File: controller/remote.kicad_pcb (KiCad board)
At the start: 2 copper layers, 69 x 58.7 mm, 32 parts, among them J1 Conn_01x03, J2 Debug, J4 Conn_01x06, J8 Conn_01x08, J9 Conn_01x08, Q1 MMBT3904, Q2 MMBT3904, U1 74HC165, U2 74HC165, U3 NRF24L01_Breakout, U4 ADS7828, U5 ESP32-WROOM-32U, U6 MC130VX

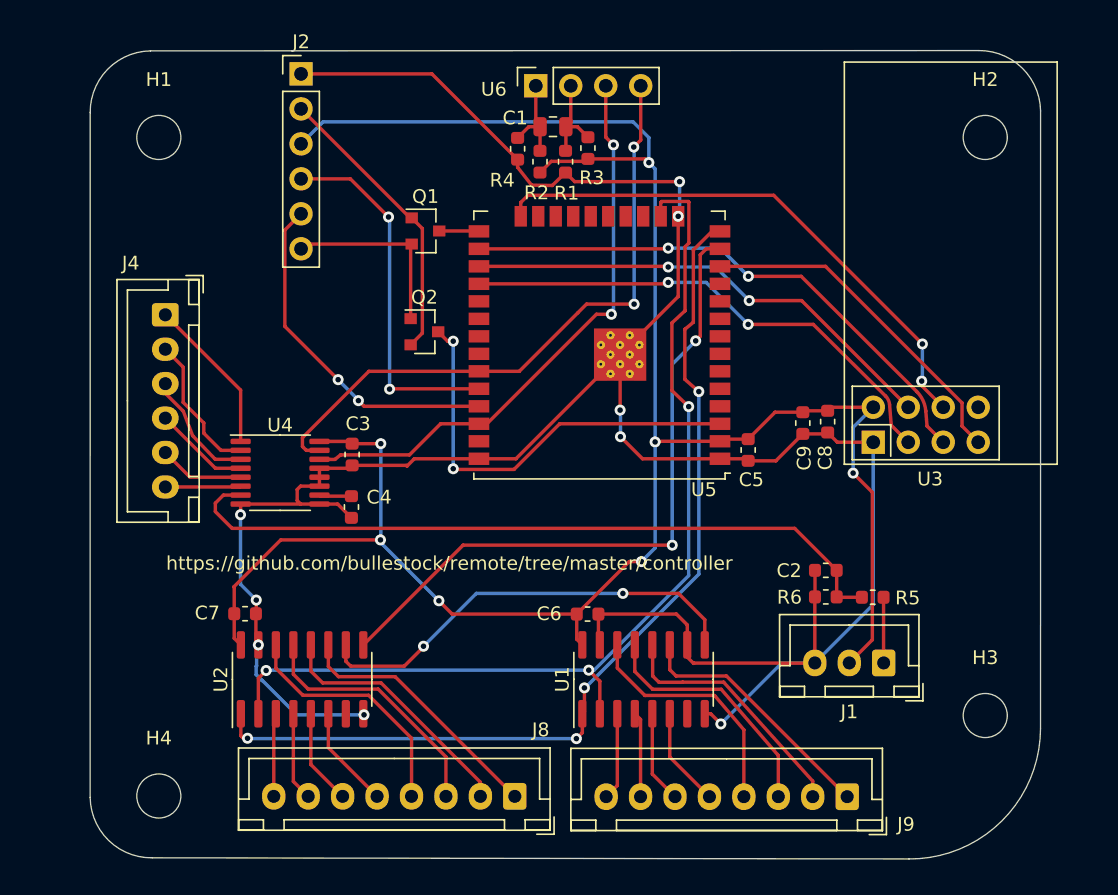
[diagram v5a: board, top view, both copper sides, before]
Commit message: Fix capacitor values.
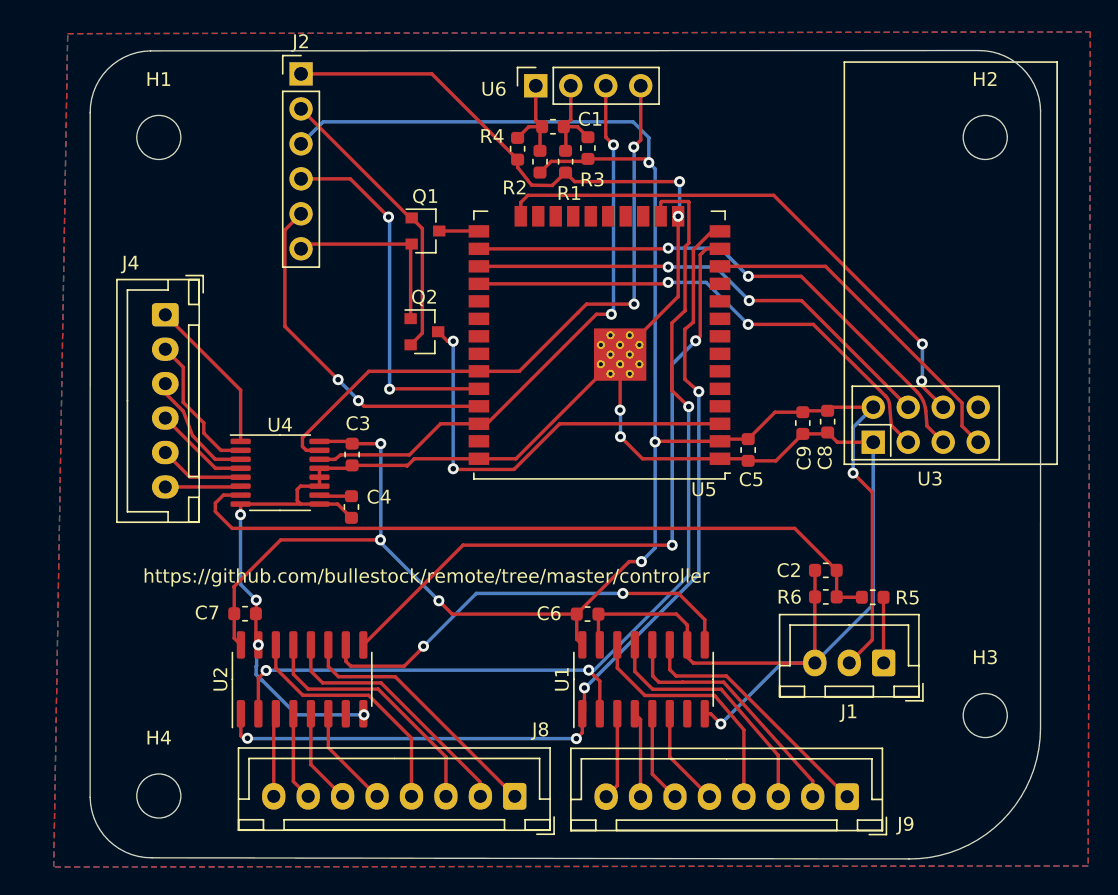
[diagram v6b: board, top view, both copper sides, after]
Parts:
- C1: footprint Capacitor_SMD:C_0805_2012Metric -> Capacitor_SMD:C_0603_1608Metric
- R1, R2: footprint Capacitor_SMD:C_0603_1608Metric -> Resistor_SMD:R_0603_1608Metric
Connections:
- C1 pad 1: Net-(U6-GND) -> Net-(U6-2)
- C1 pad 2: Net-(U6-VDD) -> Net-(U6-1)
- R1 pad 1: Net-(U6-GND) -> Net-(U6-2)
- R2 pad 1: Net-(U6-VDD) -> Net-(U6-1)
- R3 pad 1: Net-(U6-GND) -> Net-(U6-2)
- R4 pad 1: Net-(U6-VDD) -> Net-(U6-1)
- U4 pad 14: SCL -> DISP_SCL
- U4 pad 15: SDA -> DISP_SDA
- U5 pad 33: SDA -> DISP_SDA
- U5 pad 36: SCL -> DISP_SCL
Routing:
- net SDA: track 46.2 -> 0.00 mm, vias 2 -> 0
- net DISP_SDA: track 0.00 -> 46.2 mm, vias 0 -> 2
- net SCL: track 42.4 -> 0.00 mm, vias 2 -> 0
- net DISP_SCL: track 0.00 -> 42.4 mm, vias 0 -> 2
- net Net-(U6-1): track 0.00 -> 6.88 mm
- net Net-(U6-2): track 0.00 -> 6.86 mm
- net Net-(U6-VDD): track 6.82 -> 0.00 mm
- net Net-(U6-GND): track 6.80 -> 0.00 mm
- added copper zone on B.Cu, net GND
- added copper zone on F.Cu, net GND

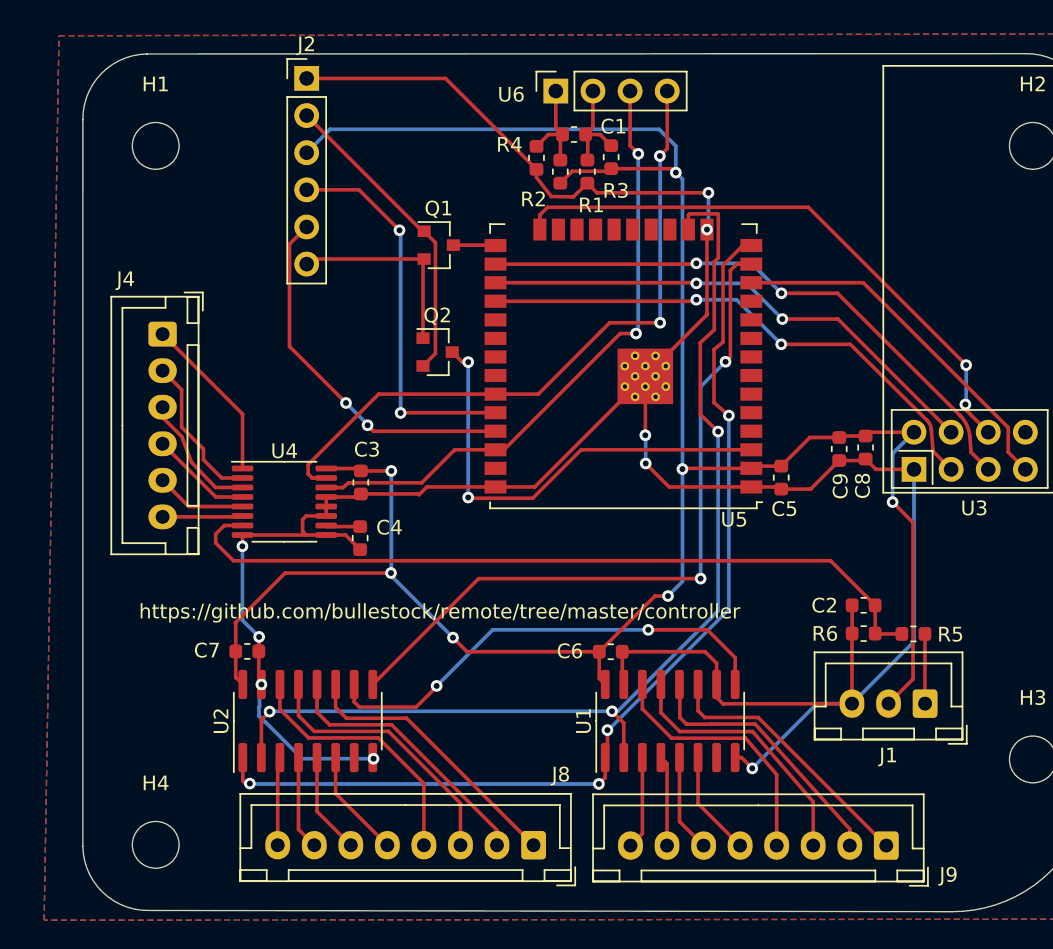
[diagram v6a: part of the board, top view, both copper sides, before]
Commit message: Add switches, regulator, etc.
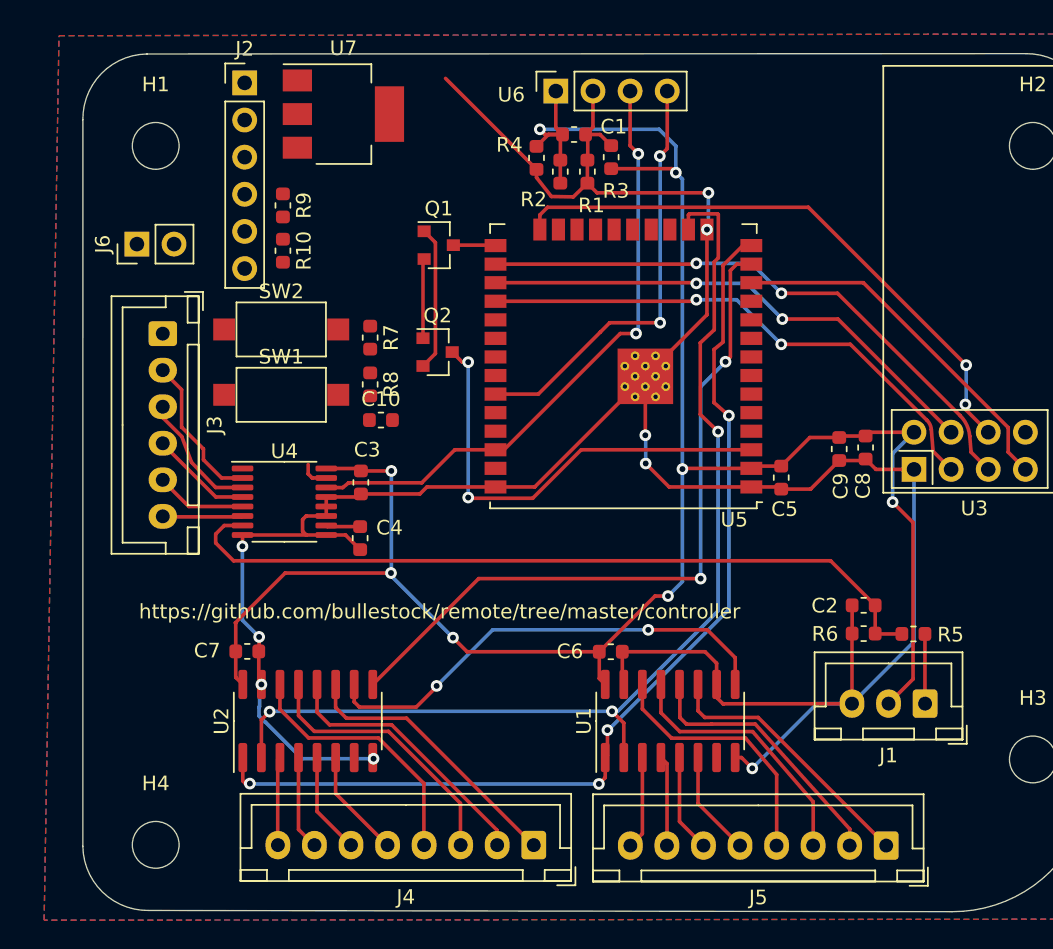
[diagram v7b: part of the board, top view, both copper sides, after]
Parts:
- removed J8, J9: Conn_01x08, Connector_JST:JST_XH_B08B-XH-A_1x08_P2.50mm_Vertical
- added C10: 100n, Capacitor_SMD:C_0603_1608Metric, F.Cu at (281.4, 117.8)
- added J3: Conn_01x06, Connector_JST:JST_XH_B06B-XH-A_1x06_P2.50mm_Vertical, F.Cu at (266.5, 111.8)
- added J5: Conn_01x08, Connector_JST:JST_XH_B08B-XH-A_1x08_P2.50mm_Vertical, F.Cu at (316.0, 146.9)
- added J6: Jumper, Connector_PinHeader_2.54mm:PinHeader_1x02_P2.54mm_Vertical, F.Cu at (264.7, 105.7)
- added R10: 2k2, Resistor_SMD:R_0603_1608Metric, F.Cu at (274.7, 106.2)
- added R7: 10k, Resistor_SMD:R_0603_1608Metric, F.Cu at (280.7, 112.1)
- added R8: 10k, Resistor_SMD:R_0603_1608Metric, F.Cu at (280.7, 115.3)
- added R9: 1k2, Resistor_SMD:R_0603_1608Metric, F.Cu at (274.7, 103.1)
- added SW1: SW_SPST, Button_Switch_SMD:SW_SPST_CK_RS282G05A3, F.Cu at (274.6, 116.0)
- added SW2: SW_SPST, Button_Switch_SMD:SW_SPST_CK_RS282G05A3, F.Cu at (274.6, 111.6)
- added U7: AMS1117-3.3, Package_TO_SOT_SMD:SOT-223-3_TabPin2, F.Cu at (278.8, 96.8)
- C5: value C -> 1u
- J4: value Conn_01x06 -> Conn_01x08; footprint Connector_JST:JST_XH_B06B-XH-A_1x06_P2.50mm_Vertical -> Connector_JST:JST_XH_B08B-XH-A_1x08_P2.50mm_Vertical
- moved J4 43.2 mm to (291.9, 146.8), turned to 180 degrees
- moved J2 4.25 mm to (272.1, 94.7)
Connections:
- net DISP_SCL renamed SCL
- net DISP_SDA renamed SDA
- net ~{DTR} renamed DTR
- net ~{RTS} renamed RTS
- J2 pad 3: +3V3 -> Net-(J2-Pin_3)
- J2 pad 4: MCU_RX0 -> Net-(J2-Pin_4)
- R1 pad 1: Net-(U6-2) -> Net-(U6-1)
- R1 pad 2: GND -> +3V3
- R2 pad 1: Net-(U6-1) -> Net-(U6-2)
- R2 pad 2: +3V3 -> GND
- U2 pad 11: Net-(J8-Pin_1) -> Net-(J4-Pin_1)
- U2 pad 12: Net-(J8-Pin_2) -> Net-(J4-Pin_2)
- U2 pad 13: Net-(J8-Pin_3) -> Net-(J4-Pin_3)
- U2 pad 14: Net-(J8-Pin_4) -> Net-(J4-Pin_4)
- U2 pad 3: Net-(J8-Pin_8) -> Net-(J4-Pin_8)
- U2 pad 4: Net-(J8-Pin_7) -> Net-(J4-Pin_7)
- U2 pad 5: Net-(J8-Pin_6) -> Net-(J4-Pin_6)
- U2 pad 6: Net-(J8-Pin_5) -> Net-(J4-Pin_5)
- U4 pad 1: Net-(J4-Pin_1) -> Net-(J3-Pin_1)
- U4 pad 2: Net-(J4-Pin_2) -> Net-(J3-Pin_2)
- U4 pad 3: Net-(J4-Pin_3) -> Net-(J3-Pin_3)
- U4 pad 4: Net-(J4-Pin_4) -> Net-(J3-Pin_4)
- U4 pad 5: Net-(J4-Pin_5) -> Net-(J3-Pin_5)
- U4 pad 6: Net-(J4-Pin_6) -> Net-(J3-Pin_6)
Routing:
- net MCU_RX0: track 26.5 -> 0.00 mm, vias 2 -> 0
- net MCU_TX0: track 25.2 -> 0.00 mm, vias 2 -> 0
- net Net-(J8-Pin_1): track 19.0 -> 0.00 mm
- net Net-(J8-Pin_2): track 19.0 -> 0.00 mm
- net Net-(J8-Pin_3): track 18.6 -> 0.00 mm
- net Net-(J8-Pin_4): track 18.3 -> 0.00 mm
- net SDA: track 46.2 -> 31.3 mm
- net Net-(J4-Pin_4): track 6.98 -> 18.3 mm
- net RTS: track 21.2 -> 10.0 mm
- net Net-(J3-Pin_2): track 0.00 -> 10.4 mm
- net +3V3: track 156.8 -> 146.4 mm, vias 7 -> 8
- net Net-(J4-Pin_3): track 8.66 -> 18.6 mm
- net Net-(J3-Pin_3): track 0.00 -> 8.66 mm
- net Net-(J4-Pin_2): track 10.4 -> 19.0 mm
- net DTR: track 13.6 -> 5.45 mm
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
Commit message: Move nRF footprint.
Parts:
- moved C8 5.00 mm to (314.6, 124.6)
- moved C9 5.00 mm to (312.8, 124.7)
- moved U3 5.00 mm to (317.9, 126.1)
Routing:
- net +3V3: track 146.4 -> 123.6 mm, vias 8 -> 7
- net GND: track 186.9 -> 170.3 mm
- net MISO: track 25.0 -> 32.3 mm, vias 0 -> 2
- net SCK: track 40.5 -> 45.6 mm
- net CE: track 36.9 -> 42.0 mm
- net CS: track 35.4 -> 40.4 mm
- net MOSI: track 40.1 -> 45.1 mm, vias 2 -> 0
